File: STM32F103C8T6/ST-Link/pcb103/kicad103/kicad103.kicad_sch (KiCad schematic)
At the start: 30 parts, among them J1 0480372200, J2 Conn_01x02_Socket, J3 Conn_02x05_Odd_Even, J5 Conn_01x16_Pin, J7 Conn_01x04_Pin, J8 Conn_01x05_Socket, J9 Conn_01x17_Pin, U1 STM32F103C8T6, U2 XC6206PxxxMR, Y1 8MHz 20pF

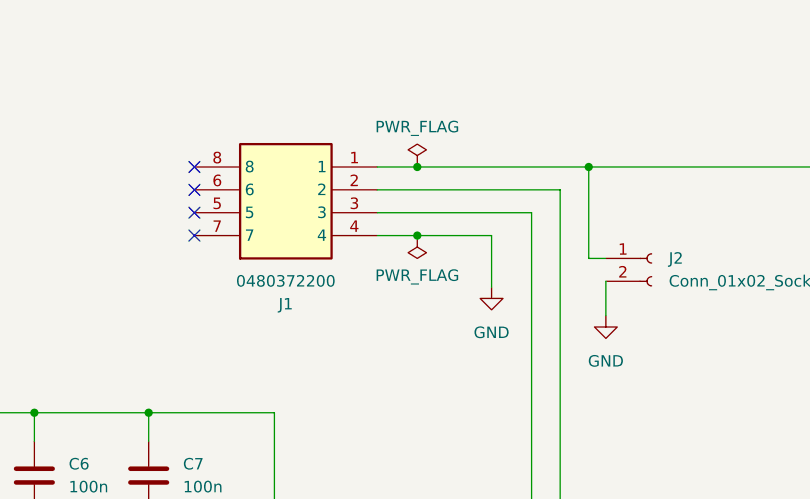
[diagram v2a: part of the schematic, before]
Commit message: Update USBA pin order
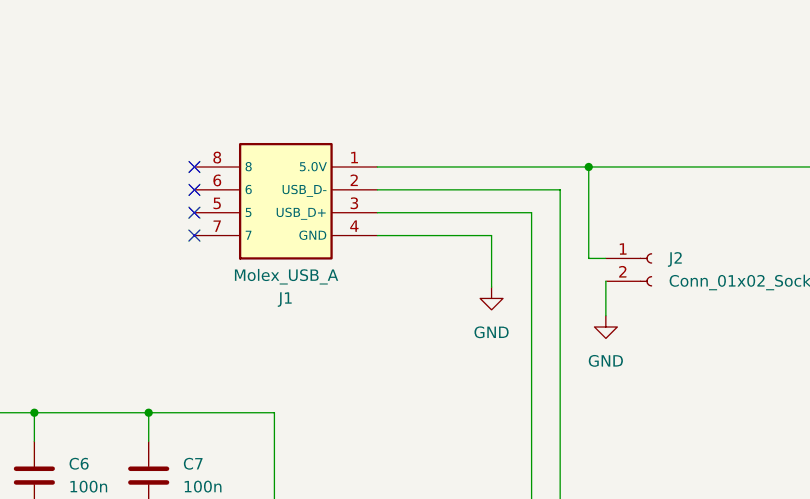
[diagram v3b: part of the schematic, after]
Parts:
- removed J1: 0480372200, Library:0480372200, symbol New_Library:0480372200
- added J1: Molex_USB_A, 0480372200, symbol MyLib:Molex_USB_A
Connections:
- net GND: now also J1.4 (GND)
- net USB_D+: now also J1.3 (USB_D+)
- net USB_D-: now also J1.2 (USB_D-)
- net at C1.1, J2.1 (Pin_1), U2.3 (VI): now also J1.1 (5.0V)
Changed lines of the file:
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@@
   (junction (at 156.845 28.575) (diameter 0) (color 0 0 0 0)
   )
-  (junction (at 137.795 36.195) (diameter 0) (color 0 0 0 0)
-  )
   (junction (at 196.85 42.545) (diameter 0) (color 0 0 0 0)
   )
@@
   )
   (junction (at 69.215 68.58) (diameter 0) (color 0 0 0 0)
-  )
-  (junction (at 137.795 28.575) (diameter 0) (color 0 0 0 0)
   )
   (junction (at 82.55 55.88) (diameter 0) (color 0 0 0 0)
@@
     (stroke (width 0) (type default))
   )
-  (wire (pts (xy 137.795 36.195) (xy 146.05 36.195))
-    (stroke (width 0) (type default))
-  )
   (wire (pts (xy 86.995 81.915) (xy 89.535 81.915))
     (stroke (width 0) (type default))
@@
     (stroke (width 0) (type default))
   )
-  (wire (pts (xy 137.795 28.575) (xy 156.845 28.575))
-    (stroke (width 0) (type default))
-  )
   (wire (pts (xy 133.35 33.655) (xy 150.495 33.655))
     (stroke (width 0) (type default))
@@
     (stroke (width 0) (type default))
   )
-  (wire (pts (xy 133.35 36.195) (xy 137.795 36.195))
+  (wire (pts (xy 133.35 36.195) (xy 146.05 36.195))
     (stroke (width 0) (type default))
   )
@@
     (stroke (width 0) (type default))
   )
-  (wire (pts (xy 133.35 28.575) (xy 137.795 28.575))
+  (wire (pts (xy 133.35 28.575) (xy 156.845 28.575))
     (stroke (width 0) (type default))
   )
@@
     )
   )
+  (symbol (lib_id "MyLib:Molex_USB_A") (at 113.03 36.195 0) (mirror x) (unit 1)
+    (in_bom yes) (on_board yes) (dnp no)
+    (property "Reference" "J1" (at 123.19 43.18 0)
+      (effects (font (size 1.27 1.27)))
+    )
+    (property "Value" "Molex_USB_A" (at 123.19 40.64 0)
+      (effects (font (size 1.27 1.27)))
+    )
+    (property "Footprint" "0480372200" (at 129.54 -58.725 0)
+      (effects (font (size 1.27 1.27)) (justify left top) hide)
+    )
+    (property "Datasheet" "https://www.molex.com/pdm_docs/sd/480372200_sd.pdf" (at 129.54 -158.725 0)
+      (effects (font (size 1.27 1.27)) (justify left top) hide)
+    )
+    (property "Height" "4" (at 129.54 -358.725 0)
+      (effects (font (size 1.27 1.27)) (justify left top) hide)
+    )
+    (property "Manufacturer_Name" "Molex" (at 129.54 -458.725 0)
+      (effects (font (size 1.27 1.27)) (justify left top) hide)
+    )
+    (property "Manufacturer_Part_Number" "0480372200" (at 129.54 -558.725 0)
+      (effects (font (size 1.27 1.27)) (justify left top) hide)
+    )
+    (property "Mouser Part Number" "N/A" (at 129.54 -658.725 0)
+      (effects (font (size 1.27 1.27)) (justify left top) hide)
+    )
+    (property "Mouser Price/Stock" "https://www.mouser.co.uk/ProductDetail/Molex/0480372200?qs=PBcRNPEHKspH5weIJRN3iw%3D%3D" (at 129.54 -758.725 0)
+      (effects (font (size 1.27 1.27)) (justify left top) hide)
+    )
+    (property "Arrow Part Number" "0480372200" (at 129.54 -858.725 0)
+      (effects (font (size 1.27 1.27)) (justify left top) hide)
+    )
+    (property "Arrow Price/Stock" "https://www.arrow.com/en/products/0480372200/molex?region=nac" (at 129.54 -958.725 0)
+      (effects (font (size 1.27 1.27)) (justify left top) hide)
+    )
+    (pin "1")
+    (pin "2")
+    (pin "3")
+    (pin "4")
+    (pin "5")
+    (pin "6")
+    (pin "7")
+    (pin "8")
+    (instances
+      (project "kicad103"
+        (path "/185c057b-9149-49f2-8708-a9b3e40a18db"
+          (reference "J1") (unit 1)
+        )
+      )
+    )
+  )
   (symbol (lib_id "Connector:Conn_01x04_Pin") (at 241.3 146.685 0) (unit 1)
     (in_bom yes) (on_board yes) (dnp no) (fields_autoplaced)
@@
         (path "/185c057b-9149-49f2-8708-a9b3e40a18db"
           (reference "#PWR020") (unit 1)
-        )
-      )
-    )
-  )
-  (symbol (lib_id "power:PWR_FLAG") (at 137.795 28.575 0) (unit 1)
-    (in_bom yes) (on_board yes) (dnp no) (fields_autoplaced)
-    (property "Reference" "#FLG01" (at 137.795 26.67 0)
-      (effects (font (size 1.27 1.27)) hide)
-    )
-    (property "Value" "PWR_FLAG" (at 137.795 24.13 0)
-      (effects (font (size 1.27 1.27)))
-    )
-    (property "Footprint" "" (at 137.795 28.575 0)
-      (effects (font (size 1.27 1.27)) hide)
-    )
-    (property "Datasheet" "~" (at 137.795 28.575 0)
-      (effects (font (size 1.27 1.27)) hide)
-    )
-    (pin "1")
-    (instances
-      (project "kicad103"
-        (path "/185c057b-9149-49f2-8708-a9b3e40a18db"
-          (reference "#FLG01") (unit 1)
         )
       )
@@
     )
   )
-  (symbol (lib_id "New_Library:0480372200") (at 113.03 36.195 0) (mirror x) (unit 1)
-    (in_bom yes) (on_board yes) (dnp no)
-    (property "Reference" "J1" (at 123.19 43.815 0)
-      (effects (font (size 1.27 1.27)))
-    )
-    (property "Value" "0480372200" (at 123.19 41.275 0)
-      (effects (font (size 1.27 1.27)))
-    )
-    (property "Footprint" "Library:0480372200" (at 129.54 -58.725 0)
-      (effects (font (size 1.27 1.27)) (justify left top) hide)
-    )
-    (property "Datasheet" "https://www.molex.com/pdm_docs/sd/480372200_sd.pdf" (at 129.54 -158.725 0)
-      (effects (font (size 1.27 1.27)) (justify left top) hide)
-    )
-    (property "Height" "4" (at 129.54 -358.725 0)
-      (effects (font (size 1.27 1.27)) (justify left top) hide)
-    )
-    (property "Manufacturer_Name" "Molex" (at 129.54 -458.725 0)
-      (effects (font (size 1.27 1.27)) (justify left top) hide)
-    )
-    (property "Manufacturer_Part_Number" "0480372200" (at 129.54 -558.725 0)
-      (effects (font (size 1.27 1.27)) (justify left top) hide)
-    )
-    (property "Mouser Part Number" "N/A" (at 129.54 -658.725 0)
-      (effects (font (size 1.27 1.27)) (justify left top) hide)
-    )
-    (property "Mouser Price/Stock" "https://www.mouser.co.uk/ProductDetail/Molex/0480372200?qs=PBcRNPEHKspH5weIJRN3iw%3D%3D" (at 129.54 -758.725 0)
-      (effects (font (size 1.27 1.27)) (justify left top) hide)
-    )
-    (property "Arrow Part Number" "0480372200" (at 129.54 -858.725 0)
-      (effects (font (size 1.27 1.27)) (justify left top) hide)
-    )
-    (property "Arrow Price/Stock" "https://www.arrow.com/en/products/0480372200/molex?region=nac" (at 129.54 -958.725 0)
-      (effects (font (size 1.27 1.27)) (justify left top) hide)
-    )
-    (property "JLC #" "" (at 113.03 36.195 0)
-      (effects (font (size 1.27 1.27)) hide)
-    )
-    (pin "1")
-    (pin "2")
-    (pin "3")
-    (pin "4")
-    (pin "5")
-    (pin "6")
-    (pin "7")
-    (pin "8")
-    (instances
-      (project "kicad103"
-        (path "/185c057b-9149-49f2-8708-a9b3e40a18db"
-          (reference "J1") (unit 1)
-        )
-      )
-    )
-  )
   (symbol (lib_id "Device:R") (at 50.165 133.35 0) (unit 1)
     (in_bom yes) (on_board yes) (dnp no) (fields_autoplaced)
@@
         )
       )
-    )
-  )
-  (symbol (lib_id "power:PWR_FLAG") (at 137.795 36.195 180) (unit 1)
-    (in_bom yes) (on_board yes) (dnp no) (fields_autoplaced)
-    (property "Reference" "#FLG02" (at 137.795 38.1 0)
-      (effects (font (size 1.27 1.27)) hide)
-    )
-    (property "Value" "PWR_FLAG" (at 137.795 40.64 0)
-      (effects (font (size 1.27 1.27)))
-    )
-    (property "Footprint" "" (at 137.795 36.195 0)
-      (effects (font (size 1.27 1.27)) hide)
-    )
-    (property "Datasheet" "~" (at 137.795 36.195 0)
-      (effects (font (size 1.27 1.27)) hide)
-    )
-    (pin "1")
-    (instances
-      (project "kicad103"
-        (path "/185c057b-9149-49f2-8708-a9b3e40a18db"
-          (reference "#FLG02") (unit 1)
-        )
-      )

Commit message: Remove unused libs
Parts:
- J1: footprint 0480372200 -> MyLib:Molex_USB_A
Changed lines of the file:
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@@
       (effects (font (size 1.27 1.27)))
     )
-    (property "Footprint" "0480372200" (at 129.54 -58.725 0)
+    (property "Footprint" "MyLib:Molex_USB_A" (at 129.54 -58.725 0)
       (effects (font (size 1.27 1.27)) (justify left top) hide)
     )
